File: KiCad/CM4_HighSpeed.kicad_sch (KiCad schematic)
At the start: 12 parts

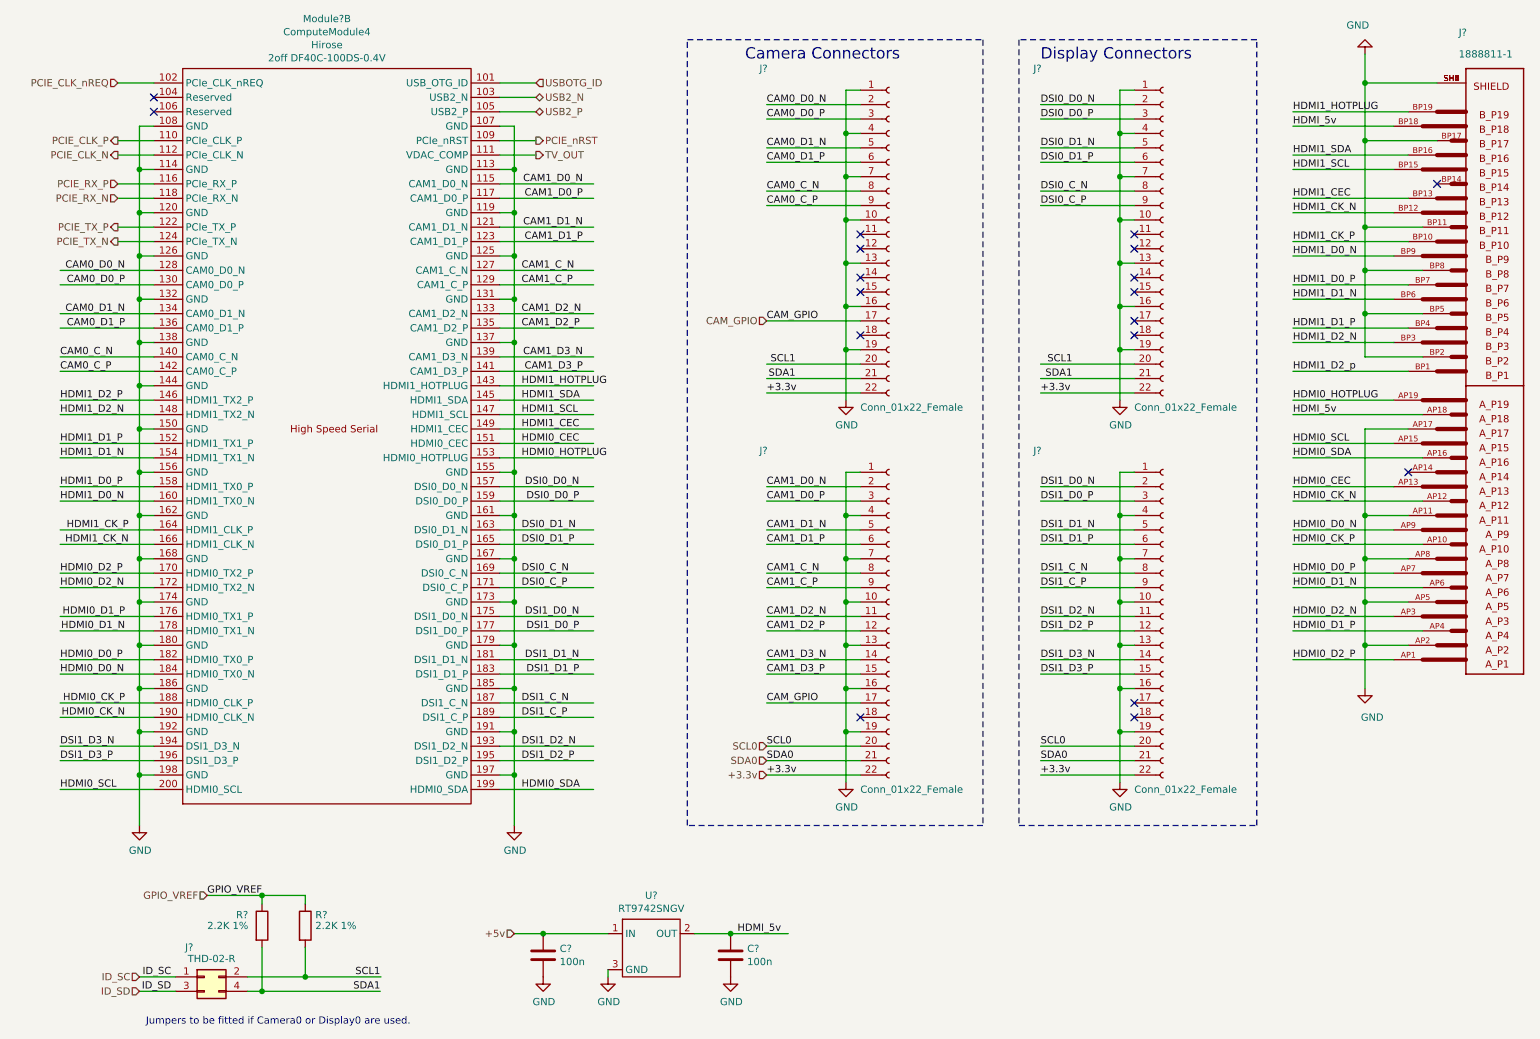
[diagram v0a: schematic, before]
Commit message: Big changes (see expanded comment)
Added new components:
USB2517-JZX USB2.0 Hub
SI-52100-002 Vertical USB2.0 A Header

Began work on USB schematic, mostly done. Needs power delivery work done
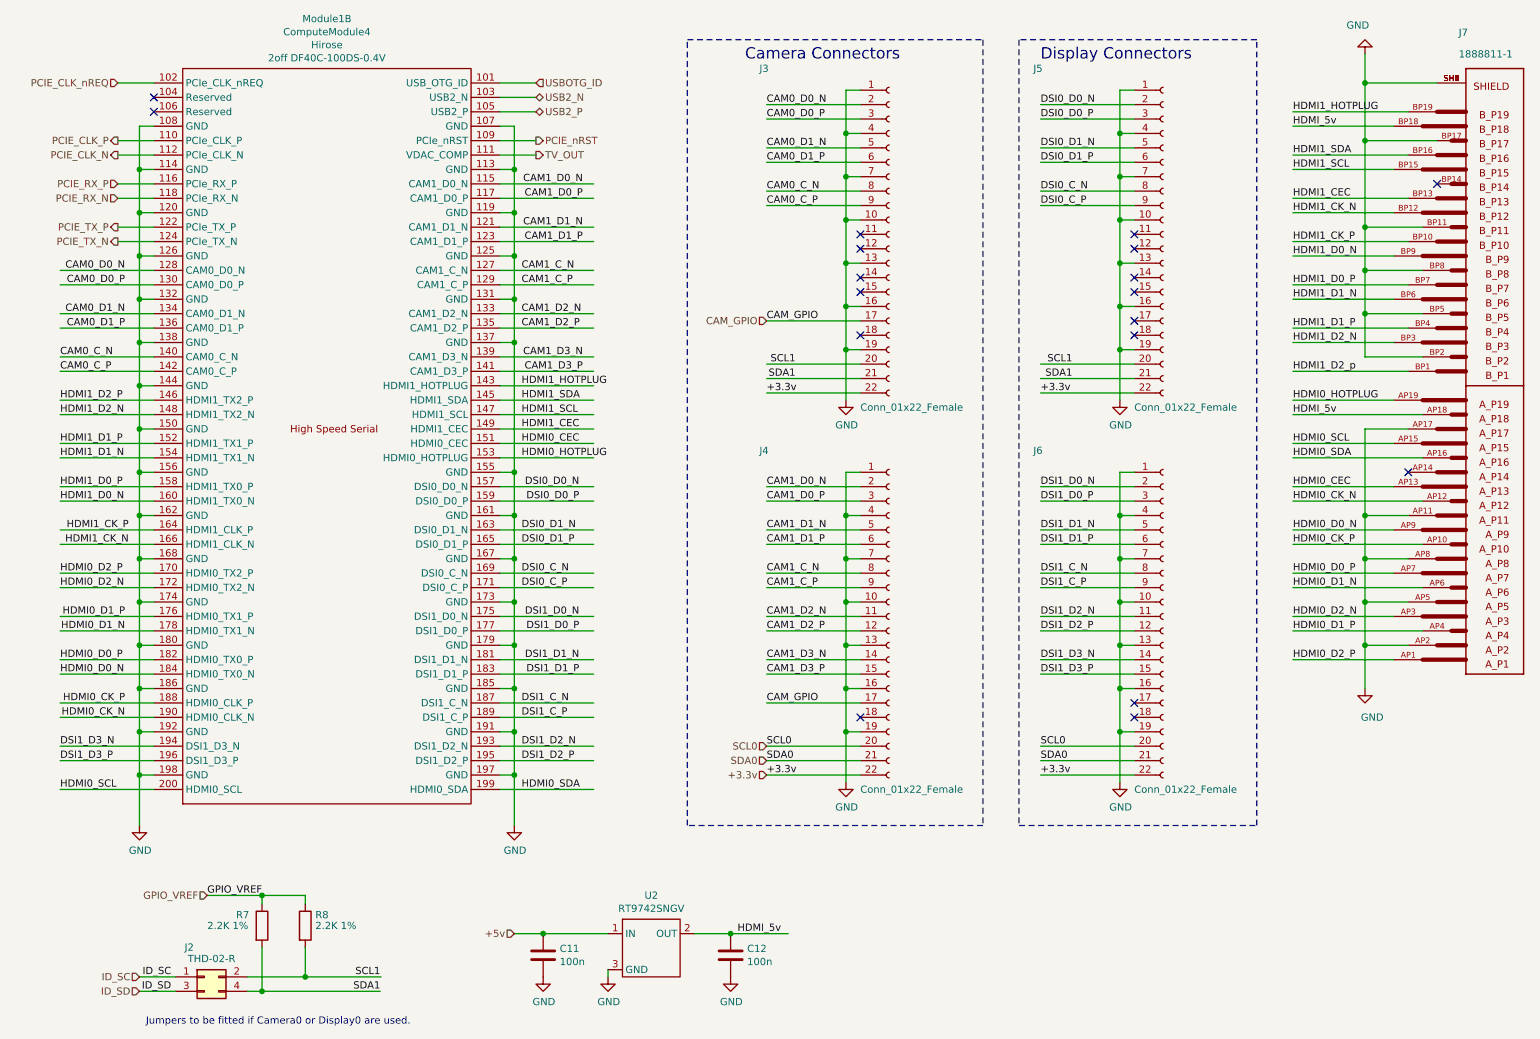
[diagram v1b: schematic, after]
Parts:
- J7: renamed from J?; footprint _TEDualHDMI:TE_1888811-1 -> CM4_MATX:TE_1888811-1
- Module1: renamed from Module?; footprint CM4IO:Raspberry-Pi-4-Compute-Module -> CM4_MATX:Raspberry-Pi-4-Compute-Module
- gave numbers to parts that had none: 10
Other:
- company: (none) -> TheGuyDanish
- title: (none) -> CM4 HighSpeed Connectors
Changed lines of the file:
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@@
 (kicad_sch (version 20200828) (generator eeschema)
-  (page 2 4)
+  (page 3 5)
   (paper "A4")
+  (title_block
+    (title "CM4 HighSpeed Connectors")
+    (date "2020-11-14")
+    (rev "0.1")
+    (company "TheGuyDanish")
+    (comment 1 "https://github.com/theguydanish/cm4_matx")
+  )
   (junction (at 35.56 40.64) (diameter 1.016) (color 0 0 0 0))
   (junction (at 35.56 48.26) (diameter 1.016) (color 0 0 0 0))
@@
   (junction (at 251.46 116.84) (diameter 1.016) (color 0 0 0 0))
   (junction (at 251.46 124.46) (diameter 1.016) (color 0 0 0 0))
+  (no_connect (at 210.82 134.62))
+  (no_connect (at 162.56 69.85))
+  (no_connect (at 210.82 52.07))
+  (no_connect (at 210.82 69.85))
+  (no_connect (at 210.82 62.23))
   (no_connect (at 210.82 54.61))
   (no_connect (at 162.56 59.69))
+  (no_connect (at 264.16 43.18))
+  (no_connect (at 162.56 62.23))
+  (no_connect (at 210.82 59.69))
+  (no_connect (at 162.56 54.61))
+  (no_connect (at 162.56 137.16))
+  (no_connect (at 162.56 52.07))
   (no_connect (at 259.08 93.98))
-  (no_connect (at 162.56 52.07))
-  (no_connect (at 162.56 62.23))
-  (no_connect (at 264.16 43.18))
-  (no_connect (at 162.56 54.61))
-  (no_connect (at 210.82 134.62))
+  (no_connect (at 210.82 67.31))
+  (no_connect (at 210.82 137.16))
   (no_connect (at 38.1 30.48))
   (no_connect (at 38.1 27.94))
-  (no_connect (at 210.82 52.07))
-  (no_connect (at 210.82 137.16))
-  (no_connect (at 210.82 62.23))
-  (no_connect (at 162.56 69.85))
-  (no_connect (at 210.82 59.69))
-  (no_connect (at 210.82 67.31))
-  (no_connect (at 210.82 69.85))
-  (no_connect (at 162.56 137.16))
   (wire (pts (xy 21.59 73.66) (xy 38.1 73.66))
     (stroke (width 0) (type solid) (color 0 0 0 0))
@@
   (symbol (lib_id "power:GND") (at 35.56 156.21 0) (unit 1)
     (in_bom yes) (on_board yes)
-    (property "Reference" "#PWR?" (id 0) (at 35.56 162.56 0)
+    (property "Reference" "#PWR0115" (id 0) (at 35.56 162.56 0)
       (effects (font (size 1.27 1.27)) hide)
     )
@@
   (symbol (lib_id "power:GND") (at 101.6 156.21 0) (unit 1)
     (in_bom yes) (on_board yes)
-    (property "Reference" "#PWR?" (id 0) (at 101.6 162.56 0)
+    (property "Reference" "#PWR0112" (id 0) (at 101.6 162.56 0)
       (effects (font (size 1.27 1.27)) hide)
     )
@@
   (symbol (lib_id "power:GND") (at 106.68 182.88 0) (unit 1)
     (in_bom yes) (on_board yes)
-    (property "Reference" "#PWR?" (id 0) (at 106.68 189.23 0)
+    (property "Reference" "#PWR0116" (id 0) (at 106.68 189.23 0)
       (effects (font (size 1.27 1.27)) hide)
     )
@@
   (symbol (lib_id "power:GND") (at 118.11 182.88 0) (unit 1)
     (in_bom yes) (on_board yes)
-    (property "Reference" "#PWR?" (id 0) (at 118.11 189.23 0)
+    (property "Reference" "#PWR0113" (id 0) (at 118.11 189.23 0)
       (effects (font (size 1.27 1.27)) hide)
     )
@@
   (symbol (lib_id "power:GND") (at 139.7 182.88 0) (unit 1)
     (in_bom yes) (on_board yes)
-    (property "Reference" "#PWR?" (id 0) (at 139.7 189.23 0)
+    (property "Reference" "#PWR0114" (id 0) (at 139.7 189.23 0)
       (effects (font (size 1.27 1.27)) hide)
     )
@@
   (symbol (lib_id "power:GND") (at 160.02 81.28 0) (unit 1)
     (in_bom yes) (on_board yes)
-    (property "Reference" "#PWR?" (id 0) (at 160.02 87.63 0)
+    (property "Reference" "#PWR0110" (id 0) (at 160.02 87.63 0)
       (effects (font (size 1.27 1.27)) hide)
     )
@@
   (symbol (lib_id "power:GND") (at 160.02 148.59 0) (unit 1)
     (in_bom yes) (on_board yes)
-    (property "Reference" "#PWR?" (id 0) (at 160.02 154.94 0)
+    (property "Reference" "#PWR0111" (id 0) (at 160.02 154.94 0)
       (effects (font (size 1.27 1.27)) hide)
     )
@@
   (symbol (lib_id "power:GND") (at 208.28 81.28 0) (unit 1)
     (in_bom yes) (on_board yes)
-    (property "Reference" "#PWR?" (id 0) (at 208.28 87.63 0)
+    (property "Reference" "#PWR0120" (id 0) (at 208.28 87.63 0)
       (effects (font (size 1.27 1.27)) hide)
     )
@@
   (symbol (lib_id "power:GND") (at 208.28 148.59 0) (unit 1)
     (in_bom yes) (on_board yes)
-    (property "Reference" "#PWR?" (id 0) (at 208.28 154.94 0)
+    (property "Reference" "#PWR0118" (id 0) (at 208.28 154.94 0)
       (effects (font (size 1.27 1.27)) hide)
     )
@@
   (symbol (lib_id "power:GND") (at 251.46 20.32 180) (unit 1)
     (in_bom yes) (on_board yes)
-    (property "Reference" "#PWR?" (id 0) (at 251.46 13.97 0)
+    (property "Reference" "#PWR0119" (id 0) (at 251.46 13.97 0)
       (effects (font (size 1.27 1.27)) hide)
     )
@@
   (symbol (lib_id "power:GND") (at 251.46 132.08 0) (unit 1)
     (in_bom yes) (on_board yes)
-    (property "Reference" "#PWR?" (id 0) (at 251.46 138.43 0)
+    (property "Reference" "#PWR0117" (id 0) (at 251.46 138.43 0)
       (effects (font (size 1.27 1.27)) hide)
     )
@@
   (symbol (lib_id "Device:R") (at 57.15 173.863 0) (unit 1)
     (in_bom yes) (on_board yes)
-    (property "Reference" "R?" (id 0) (at 52.578 171.958 0)
+    (property "Reference" "R7" (id 0) (at 52.578 171.958 0)
       (effects (font (size 1.27 1.27)) (justify left))
     )
@@
   (symbol (lib_id "Device:R") (at 64.77 173.863 0) (unit 1)
     (in_bom yes) (on_board yes)
-    (property "Reference" "R?" (id 0) (at 66.548 171.958 0)
+    (property "Reference" "R8" (id 0) (at 66.548 171.958 0)
       (effects (font (size 1.27 1.27)) (justify left))
     )
@@
   (symbol (lib_id "Device:C") (at 106.68 179.07 0) (unit 1)
     (in_bom yes) (on_board yes)
-    (property "Reference" "C?" (id 0) (at 109.601 177.9016 0)
+    (property "Reference" "C11" (id 0) (at 109.601 177.9016 0)
       (effects (font (size 1.27 1.27)) (justify left))
     )
@@
   (symbol (lib_id "Device:C") (at 139.7 179.07 0) (unit 1)
     (in_bom yes) (on_board yes)
-    (property "Reference" "C?" (id 0) (at 142.621 177.9016 0)
+    (property "Reference" "C12" (id 0) (at 142.621 177.9016 0)
       (effects (font (size 1.27 1.27)) (justify left))
     )
@@
   (symbol (lib_id "Connector_Generic:Conn_02x02_Odd_Even") (at 46.99 182.88 0) (unit 1)
     (in_bom yes) (on_board yes)
-    (property "Reference" "J?" (id 0) (at 44.323 177.673 0))
+    (property "Reference" "J2" (id 0) (at 44.323 177.673 0))
     (property "Value" "THD-02-R" (id 1) (at 48.26 179.6796 0))
     (property "Footprint" "Connector_PinHeader_2.54mm:PinHeader_2x02_P2.54mm_Vertical" (id 2) (at 46.99 182.88 0)
@@
   (symbol (lib_id "CM4_MATX:RT9742SNGV") (at 123.19 179.07 0) (unit 1)
     (in_bom yes) (on_board yes)
-    (property "Reference" "U?" (id 0) (at 125.73 168.529 0))
+    (property "Reference" "U2" (id 0) (at 125.73 168.529 0))
     (property "Value" "RT9742SNGV" (id 1) (at 125.73 170.8404 0))
     (property "Footprint" "Package_TO_SOT_SMD:SOT-23" (id 2) (at 123.19 179.07 0)
@@
   (symbol (lib_id "Connector:Conn_01x22_Female") (at 167.64 52.07 0) (unit 1)
     (in_bom yes) (on_board yes)
-    (property "Reference" "J?" (id 0) (at 144.78 22.86 0)
+    (property "Reference" "J3" (id 0) (at 144.78 22.86 0)
       (effects (font (size 1.27 1.27)) (justify left))
     )
@@
   (symbol (lib_id "Connector:Conn_01x22_Female") (at 167.64 119.38 0) (unit 1)
     (in_bom yes) (on_board yes)
-    (property "Reference" "J?" (id 0) (at 144.78 90.17 0)
+    (property "Reference" "J4" (id 0) (at 144.78 90.17 0)
       (effects (font (size 1.27 1.27)) (justify left))
     )
@@
   (symbol (lib_id "Connector:Conn_01x22_Female") (at 215.9 52.07 0) (unit 1)
     (in_bom yes) (on_board yes)
-    (property "Reference" "J?" (id 0) (at 193.04 22.86 0)
+    (property "Reference" "J5" (id 0) (at 193.04 22.86 0)
       (effects (font (size 1.27 1.27)) (justify left))
     )
@@
   (symbol (lib_id "Connector:Conn_01x22_Female") (at 215.9 119.38 0) (unit 1)
     (in_bom yes) (on_board yes)
-    (property "Reference" "J?" (id 0) (at 193.04 90.17 0)
+    (property "Reference" "J6" (id 0) (at 193.04 90.17 0)
       (effects (font (size 1.27 1.27)) (justify left))
     )
@@
   (symbol (lib_id "CM4_MATX:1888811-1") (at 269.24 78.74 180) (unit 1)
     (in_bom yes) (on_board yes)
-    (property "Reference" "J?" (id 0) (at 267.97 16.51 0)
+    (property "Reference" "J7" (id 0) (at 267.97 16.51 0)
       (effects (font (size 1.27 1.27)) (justify right))
     )
@@
       (effects (font (size 1.27 1.27)) (justify right))
     )
-    (property "Footprint" "_TEDualHDMI:TE_1888811-1" (id 2) (at 269.24 78.74 0)
+    (property "Footprint" "CM4_MATX:TE_1888811-1" (id 2) (at 269.24 78.74 0)
       (effects (font (size 1.27 1.27)) (justify left bottom) hide)
     )
@@
   (symbol (lib_id "CM4_MATX:ComputeModule4-CM4") (at -71.12 86.36 0) (unit 2)
     (in_bom yes) (on_board yes)
-    (property "Reference" "Module?" (id 0) (at 68.58 14.097 0))
+    (property "Reference" "Module1" (id 0) (at 68.58 14.097 0))
     (property "Value" "ComputeModule4" (id 1) (at 68.58 16.4084 0))
-    (property "Footprint" "CM4IO:Raspberry-Pi-4-Compute-Module" (id 2) (at 71.12 113.03 0)
-      (effects (font (size 1.27 1.27)) hide)
-    )
+    (property "Footprint" "CM4_MATX:Raspberry-Pi-4-Compute-Module" (id 2) (at 71.12 113.03 0)
+      (effects (font (size 1.27 1.27)) hide)
+    )
